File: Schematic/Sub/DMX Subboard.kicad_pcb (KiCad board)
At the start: 2 copper layers, 55.5 x 33.7 mm, 7 parts, among them J1 OLED, J2 Connector, SW1 Back, SW2 Up, SW3 Down, SW4 Confirm

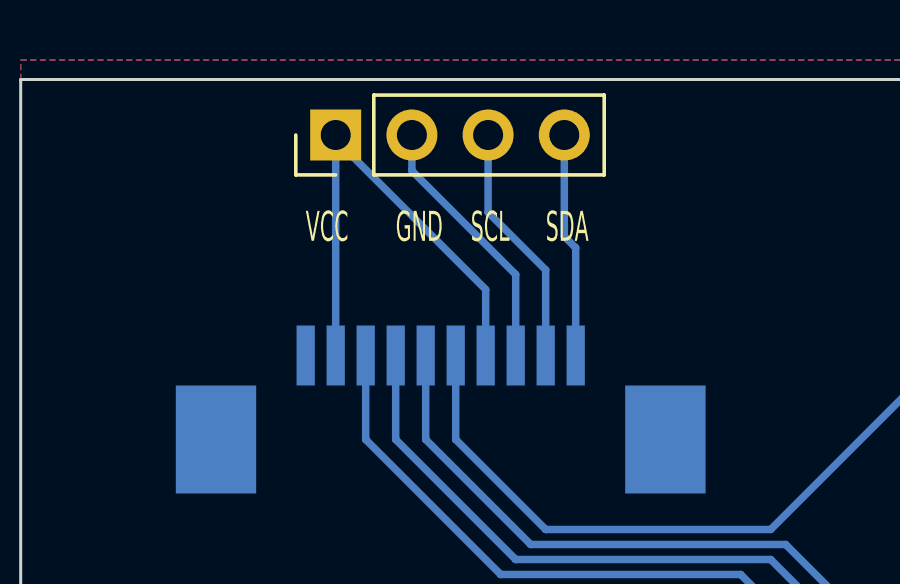
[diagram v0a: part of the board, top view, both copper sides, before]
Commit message: First OLED support
- SSD1306 support added
- OLED menu added (wip)
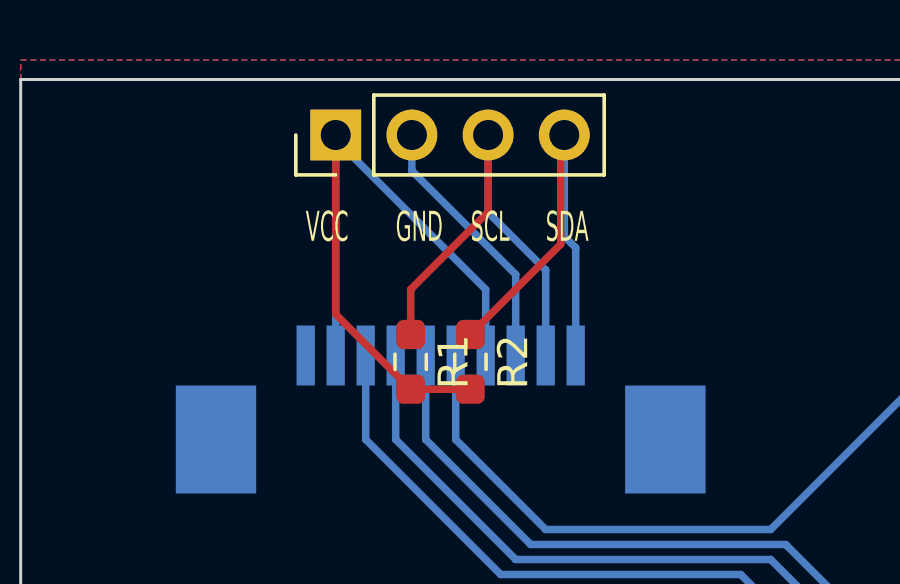
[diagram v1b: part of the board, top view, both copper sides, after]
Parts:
- added R1: 4K7, Resistor_SMD:R_0603_1608Metric_Pad0.98x0.95mm_HandSolder, F.Cu at (45.5, 44.4)
- added R2: 4K7, Resistor_SMD:R_0603_1608Metric_Pad0.98x0.95mm_HandSolder, F.Cu at (47.5, 44.4)
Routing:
- net +3.3V: track 16.8 -> 28.3 mm
- net /SDA: track 7.51 -> 15.5 mm
- net /SCL: track 8.15 -> 15.9 mm
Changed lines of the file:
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@@
+    )
+  )
+  (footprint "Resistor_SMD:R_0603_1608Metric_Pad0.98x0.95mm_HandSolder" (layer "F.Cu")
+    (at 45.5 44.4125 -90)
+    (descr "Resistor SMD 0603 (1608 Metric), square (rectangular) end terminal, IPC_7351 nominal with elongated pad for handsoldering. (Body size source: IPC-SM-782 page 72, https://www.pcb-3d.com/wordpress/wp-content/uploads/ipc-sm-782a_amendment_1_and_2.pdf), generated with kicad-footprint-generator")
+    (tags "resistor handsolder")
+    (property "Sheetfile" "DMX Subboard.kicad_sch")
+    (property "Sheetname" "")
+    (property "ki_description" "Resistor")
+    (property "ki_keywords" "R res resistor")
+    (attr smd)
+    (fp_text reference "R1" (at 0 -1.43 90) (layer "F.SilkS")
+        (effects (font (size 1 1) (thickness 0.15)))
+    )
+    (fp_text value "4K7" (at 0 1.43 90) (layer "F.Fab")
+        (effects (font (size 1 1) (thickness 0.15)))
+    )
+    (fp_text user "${REFERENCE}" (at 0 0 90) (layer "F.Fab")
+        (effects (font (size 0.4 0.4) (thickness 0.06)))
+    )
+    (fp_line (start -0.254724 -0.5225) (end 0.254724 -0.5225)
+      (stroke (width 0.12) (type solid)) (layer "F.SilkS"))
+    (fp_line (start -0.254724 0.5225) (end 0.254724 0.5225)
+      (stroke (width 0.12) (type solid)) (layer "F.SilkS"))
+    (fp_line (start -1.65 -0.73) (end 1.65 -0.73)
+      (stroke (width 0.05) (type solid)) (layer "F.CrtYd"))
+    (fp_line (start -1.65 0.73) (end -1.65 -0.73)
+      (stroke (width 0.05) (type solid)) (layer "F.CrtYd"))
+    (fp_line (start 1.65 -0.73) (end 1.65 0.73)
+      (stroke (width 0.05) (type solid)) (layer "F.CrtYd"))
+    (fp_line (start 1.65 0.73) (end -1.65 0.73)
+      (stroke (width 0.05) (type solid)) (layer "F.CrtYd"))
+    (fp_line (start -0.8 -0.4125) (end 0.8 -0.4125)
+      (stroke (width 0.1) (type solid)) (layer "F.Fab"))
+    (fp_line (start -0.8 0.4125) (end -0.8 -0.4125)
+      (stroke (width 0.1) (type solid)) (layer "F.Fab"))
+    (fp_line (start 0.8 -0.4125) (end 0.8 0.4125)
+      (stroke (width 0.1) (type solid)) (layer "F.Fab"))
+    (fp_line (start 0.8 0.4125) (end -0.8 0.4125)
+      (stroke (width 0.1) (type solid)) (layer "F.Fab"))
+    (pad "1" smd roundrect (at -0.9125 0 270) (size 0.975 0.95) (layers "F.Cu" "F.Paste" "F.Mask") (roundrect_rratio 0.25)
+      (net 3 "/SCL") (pintype "passive"))
+    (pad "2" smd roundrect (at 0.9125 0 270) (size 0.975 0.95) (layers "F.Cu" "F.Paste" "F.Mask") (roundrect_rratio 0.25)
+      (net 1 "+3.3V") (pintype "passive"))
+    (model "${KICAD6_3DMODEL_DIR}/Resistor_SMD.3dshapes/R_0603_1608Metric.wrl"
+      (offset (xyz 0 0 0))
+      (scale (xyz 1 1 1))
+      (rotate (xyz 0 0 0))
+    )
+  )
+  (footprint "Resistor_SMD:R_0603_1608Metric_Pad0.98x0.95mm_HandSolder" (layer "F.Cu")
+    (at 47.49 44.4125 -90)
+    (descr "Resistor SMD 0603 (1608 Metric), square (rectangular) end terminal, IPC_7351 nominal with elongated pad for handsoldering. (Body size source: IPC-SM-782 page 72, https://www.pcb-3d.com/wordpress/wp-content/uploads/ipc-sm-782a_amendment_1_and_2.pdf), generated with kicad-footprint-generator")
+    (tags "resistor handsolder")
+    (property "Sheetfile" "DMX Subboard.kicad_sch")
+    (property "Sheetname" "")
+    (property "ki_description" "Resistor")
+    (property "ki_keywords" "R res resistor")
+    (attr smd)
+    (fp_text reference "R2" (at 0 -1.43 90) (layer "F.SilkS")
+        (effects (font (size 1 1) (thickness 0.15)))
+    )
+    (fp_text value "4K7" (at 0 1.43 90) (layer "F.Fab")
+        (effects (font (size 1 1) (thickness 0.15)))
+    )
+    (fp_text user "${REFERENCE}" (at 0 0 90) (layer "F.Fab")
+        (effects (font (size 0.4 0.4) (thickness 0.06)))
+    )
+    (fp_line (start -0.254724 -0.5225) (end 0.254724 -0.5225)
+      (stroke (width 0.12) (type solid)) (layer "F.SilkS"))
+    (fp_line (start -0.254724 0.5225) (end 0.254724 0.5225)
+      (stroke (width 0.12) (type solid)) (layer "F.SilkS"))
+    (fp_line (start -1.65 -0.73) (end 1.65 -0.73)
+      (stroke (width 0.05) (type solid)) (layer "F.CrtYd"))
+    (fp_line (start -1.65 0.73) (end -1.65 -0.73)
+      (stroke (width 0.05) (type solid)) (layer "F.CrtYd"))
+    (fp_line (start 1.65 -0.73) (end 1.65 0.73)
+      (stroke (width 0.05) (type solid)) (layer "F.CrtYd"))
+    (fp_line (start 1.65 0.73) (end -1.65 0.73)
+      (stroke (width 0.05) (type solid)) (layer "F.CrtYd"))
+    (fp_line (start -0.8 -0.4125) (end 0.8 -0.4125)
+      (stroke (width 0.1) (type solid)) (layer "F.Fab"))
+    (fp_line (start -0.8 0.4125) (end -0.8 -0.4125)
+      (stroke (width 0.1) (type solid)) (layer "F.Fab"))
+    (fp_line (start 0.8 -0.4125) (end 0.8 0.4125)
+      (stroke (width 0.1) (type solid)) (layer "F.Fab"))
+    (fp_line (start 0.8 0.4125) (end -0.8 0.4125)
+      (stroke (width 0.1) (type solid)) (layer "F.Fab"))
+    (pad "1" smd roundrect (at -0.9125 0 270) (size 0.975 0.95) (layers "F.Cu" "F.Paste" "F.Mask") (roundrect_rratio 0.25)
+      (net 4 "/SDA") (pintype "passive"))
+    (pad "2" smd roundrect (at 0.9125 0 270) (size 0.975 0.95) (layers "F.Cu" "F.Paste" "F.Mask") (roundrect_rratio 0.25)
+      (net 1 "+3.3V") (pintype "passive"))
+    (model "${KICAD6_3DMODEL_DIR}/Resistor_SMD.3dshapes/R_0603_1608Metric.wrl"
+      (offset (xyz 0 0 0))
+      (scale (xyz 1 1 1))
+      (rotate (xyz 0 0 0))
     )
   )
@@
     (effects (font (size 1 1) (thickness 0.15)) (justify left bottom))
   )
+  (segment (start 45.5 45.325) (end 43 42.825) (width 0.25) (layer "F.Cu") (net 1))
+  (segment (start 47.49 45.325) (end 45.5 45.325) (width 0.25) (layer "F.Cu") (net 1))
+  (segment (start 43 42.825) (end 43 36.85) (width 0.25) (layer "F.Cu") (net 1))
   (segment (start 48 42) (end 43 37) (width 0.25) (layer "B.Cu") (net 1))
   (segment (start 43 36.85) (end 43 44.2) (width 0.25) (layer "B.Cu") (net 1))
@@
   (segment (start 49 44.2) (end 49 41.5) (width 0.25) (layer "B.Cu") (net 2))
   (segment (start 45.54 38.04) (end 45.54 36.85) (width 0.25) (layer "B.Cu") (net 2))
+  (segment (start 45.5 42) (end 48.08 39.42) (width 0.25) (layer "F.Cu") (net 3))
+  (segment (start 45.5 43.5) (end 45.5 42) (width 0.25) (layer "F.Cu") (net 3))
+  (segment (start 48.08 39.42) (end 48.08 36.85) (width 0.25) (layer "F.Cu") (net 3))
   (segment (start 50 41.35) (end 50 44.2) (width 0.25) (layer "B.Cu") (net 3))
   (segment (start 48.08 39.43) (end 50 41.35) (width 0.25) (layer "B.Cu") (net 3))
   (segment (start 48.08 36.85) (end 48.08 39.43) (width 0.25) (layer "B.Cu") (net 3))
+  (segment (start 50.5 36.97) (end 50.62 36.85) (width 0.25) (layer "F.Cu") (net 4))
+  (segment (start 50.5 40.49) (end 50.5 36.97) (width 0.25) (layer "F.Cu") (net 4))
+  (segment (start 47.49 43.5) (end 50.5 40.49) (width 0.25) (layer "F.Cu") (net 4))
   (segment (start 51 40.61) (end 51 44.2) (width 0.25) (layer "B.Cu") (net 4))
   (segment (start 50.62 36.85) (end 50.62 40.23) (width 0.25) (layer "B.Cu") (net 4))

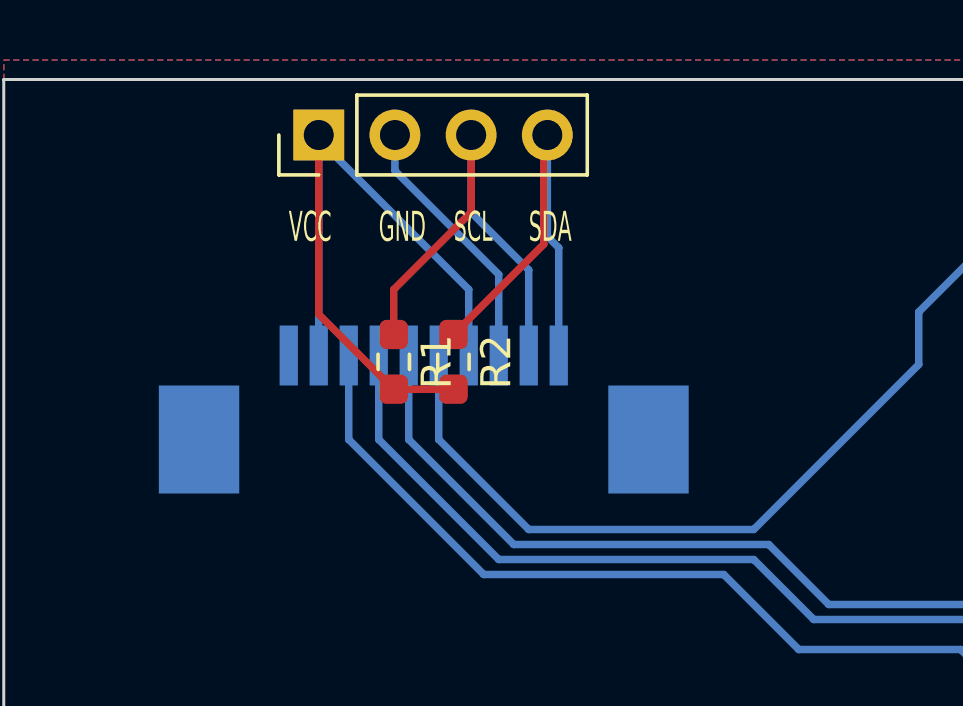
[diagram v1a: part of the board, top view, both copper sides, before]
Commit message: Added support for different OLED-pinning
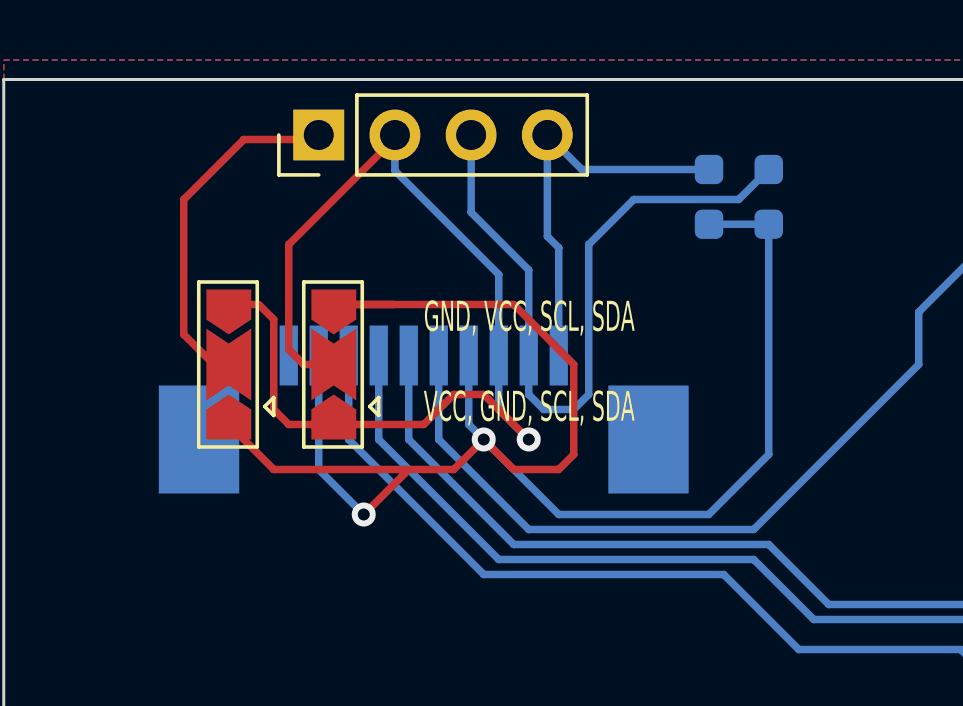
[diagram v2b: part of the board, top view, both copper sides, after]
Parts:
- added JP1: PIN 1, Jumper:SolderJumper-3_P2.0mm_Open_TrianglePad1.0x1.5mm, F.Cu at (40.0, 44.5)
- added JP2: PIN 2, Jumper:SolderJumper-3_P2.0mm_Open_TrianglePad1.0x1.5mm, F.Cu at (43.5, 44.5)
- R1, R2: moved to B.Cu
- moved R1 13.7 mm to (58.0, 38.9)
- moved R2 10.1 mm to (56.0, 38.9)
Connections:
- J1 pad 1: +3.3V -> Net-(J1-Pin_1)
- J1 pad 2: GND -> Net-(J1-Pin_2)
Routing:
- net +3.3V: track 28.3 -> 59.1 mm, vias 0 -> 2
- net GND: track 8.78 -> 26.4 mm, vias 0 -> 1
- net Net-(J1-Pin_1): track 0.00 -> 12.0 mm
- net Net-(J1-Pin_2): track 0.00 -> 10.3 mm
- net /SCL: track 15.9 -> 23.9 mm
- net /SDA: track 15.5 -> 13.5 mm
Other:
- board text added: "GND, VCC, SCL, SDA"
- board text added: "VCC, GND, SCL, SDA"
- board text removed: "GND"
- board text removed: "SCL"
- board text removed: "SDA"
- board text removed: "VCC"
